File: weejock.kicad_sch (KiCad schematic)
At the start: 44 parts, among them J2 JST-PH2, K1 PG1350, K10 PG1350, K11 PG1350, K12 PG1350, K13 PG1350, K14 PG1350, K15 PG1350, K16 PG1350, K17 PG1350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

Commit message: Beginning to assign footprints.
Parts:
- D1, D10, D11, D12, D13, D14, D15, D16, D17, D18, D19, D2, D20, D3, D4, D5, D6, D7, D8, D9: footprint (none) -> Diode_SMD:D_SOD-123
- J2: footprint (none) -> Connector_JST:JST_PH_S2B-PH-SM4-TB_1x02-1MP_P2.00mm_Horizontal
- K1, K10, K11, K12, K13, K14, K15, K16, K17, K18, K19, K2, K20, K3, K4, K5, K6, K7, K8, K9: footprint (none) -> Switch_Keyboard_Kailh:SW_Kailh_Choc_V1
- SW1: footprint (none) -> Button_Switch_SMD:SW_Push_SPST_NO_Alps_SKRK
- SW2: footprint (none) -> Button_Switch_SMD:SW_SPDT_PCM12
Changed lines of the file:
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@@
 			)
 		)
-		(property "Footprint" ""
+		(property "Footprint" "Diode_SMD:D_SOD-123"
 			(at 38.1 58.42 0)
 			(effects
@@
 			)
 		)
-		(property "Footprint" ""
+		(property "Footprint" "Switch_Keyboard_Kailh:SW_Kailh_Choc_V1"
 			(at 88.9 68.58 0)
 			(effects
@@
 			)
 		)
-		(property "Footprint" ""
+		(property "Footprint" "Switch_Keyboard_Kailh:SW_Kailh_Choc_V1"
 			(at 50.8 87.63 0)
 			(effects
@@
 			)
 		)
-		(property "Footprint" ""
+		(property "Footprint" "Diode_SMD:D_SOD-123"
 			(at 76.2 77.47 0)
 			(effects
@@
 			)
 		)
-		(property "Footprint" ""
+		(property "Footprint" "Switch_Keyboard_Kailh:SW_Kailh_Choc_V1"
 			(at 69.85 68.58 0)
 			(effects
@@
 			)
 		)
-		(property "Footprint" ""
+		(property "Footprint" "Diode_SMD:D_SOD-123"
 			(at 38.1 39.37 0)
 			(effects
@@
 			)
 		)
-		(property "Footprint" ""
+		(property "Footprint" "Button_Switch_SMD:SW_Push_SPST_NO_Alps_SKRK"
 			(at 134.62 99.06 0)
 			(effects
@@
 			)
 		)
-		(property "Footprint" ""
+		(property "Footprint" "Diode_SMD:D_SOD-123"
 			(at 38.1 77.47 0)
 			(effects
@@
 			)
 		)
-		(property "Footprint" ""
+		(property "Footprint" "Diode_SMD:D_SOD-123"
 			(at 76.2 58.42 0)
 			(effects
@@
 			)
 		)
-		(property "Footprint" ""
+		(property "Footprint" "Switch_Keyboard_Kailh:SW_Kailh_Choc_V1"
 			(at 88.9 49.53 0)
 			(effects
@@
 			)
 		)
-		(property "Footprint" ""
+		(property "Footprint" "Connector_JST:JST_PH_S2B-PH-SM4-TB_1x02-1MP_P2.00mm_Horizontal"
 			(at 190.5 107.95 0)
 			(effects
@@
 			)
 		)
-		(property "Footprint" ""
+		(property "Footprint" "Diode_SMD:D_SOD-123"
 			(at 38.1 96.52 0)
 			(effects
@@
 			)
 		)
-		(property "Footprint" ""
+		(property "Footprint" "Diode_SMD:D_SOD-123"
 			(at 95.25 39.37 0)
 			(effects
@@
 			)
 		)
-		(property "Footprint" ""
+		(property "Footprint" "Diode_SMD:D_SOD-123"
 			(at 76.2 115.57 0)
 			(effects
@@
 			)
 		)
-		(property "Footprint" ""
+		(property "Footprint" "Switch_Keyboard_Kailh:SW_Kailh_Choc_V1"
 			(at 50.8 106.68 0)
 			(effects
@@
 			)
 		)
-		(property "Footprint" ""
+		(property "Footprint" "Diode_SMD:D_SOD-123"
 			(at 95.25 77.47 0)
 			(effects
@@
 			)
 		)
-		(property "Footprint" ""
+		(property "Footprint" "Switch_Keyboard_Kailh:SW_Kailh_Choc_V1"
 			(at 69.85 49.53 0)
 			(effects
@@
 			)
 		)
-		(property "Footprint" ""
+		(property "Footprint" "Switch_Keyboard_Kailh:SW_Kailh_Choc_V1"
 			(at 50.8 68.58 0)
 			(effects
@@
 			)
 		)
-		(property "Footprint" ""
+		(property "Footprint" "Diode_SMD:D_SOD-123"
 			(at 76.2 96.52 0)
 			(effects
@@
 			)
 		)
-		(property "Footprint" ""
+		(property "Footprint" "Switch_Keyboard_Kailh:SW_Kailh_Choc_V1"
 			(at 69.85 30.48 0)
 			(effects
@@
 			)
 		)
-		(property "Footprint" ""
+		(property "Footprint" "Switch_Keyboard_Kailh:SW_Kailh_Choc_V1"
 			(at 31.75 49.53 0)
 			(effects
@@
 			)
 		)
-		(property "Footprint" ""
+		(property "Footprint" "Diode_SMD:D_SOD-123"
 			(at 57.15 96.52 0)
 			(effects
@@
 			)
 		)
-		(property "Footprint" ""
+		(property "Footprint" "Switch_Keyboard_Kailh:SW_Kailh_Choc_V1"
 			(at 50.8 30.48 0)
 			(effects
@@
 			)
 		)
-		(property "Footprint" ""
+		(property "Footprint" "Diode_SMD:D_SOD-123"
 			(at 95.25 96.52 0)
 			(effects
@@
 			)
 		)
-		(property "Footprint" ""
+		(property "Footprint" "Diode_SMD:D_SOD-123"
 			(at 57.15 58.42 0)
 			(effects
@@
 			)
 		)
-		(property "Footprint" ""
+		(property "Footprint" "Switch_Keyboard_Kailh:SW_Kailh_Choc_V1"
 			(at 31.75 68.58 0)
 			(effects
@@
 	)
 	(symbol
+		(lib_name "PG1350_1")
 		(lib_id "weejock_keyboard_parts:PG1350")
 		(at 31.75 35.56 0)
@@
 			)
 		)
-		(property "Footprint" ""
+		(property "Footprint" "Switch_Keyboard_Kailh:SW_Kailh_Choc_V1"
 			(at 31.75 30.48 0)
 			(effects
@@
 			)
 		)
-		(property "Footprint" ""
+		(property "Footprint" "Diode_SMD:D_SOD-123"
 			(at 95.25 58.42 0)
 			(effects
@@
 			)
 		)
-		(property "Footprint" ""
+		(property "Footprint" "Switch_Keyboard_Kailh:SW_Kailh_Choc_V1"
 			(at 88.9 87.63 0)
 			(effects
@@
 			)
 		)
-		(property "Footprint" ""
+		(property "Footprint" "Diode_SMD:D_SOD-123"
 			(at 57.15 77.47 0)
 			(effects
@@
 			)
 		)
-		(property "Footprint" ""
+		(property "Footprint" "Diode_SMD:D_SOD-123"
 			(at 57.15 115.57 0)
 			(effects
@@
 			)
 		)
-		(property "Footprint" ""
+		(property "Footprint" "Switch_Keyboard_Kailh:SW_Kailh_Choc_V1"
 			(at 69.85 106.68 0)
 			(effects
@@
 			)
 		)
-		(property "Footprint" ""
+		(property "Footprint" "Diode_SMD:D_SOD-123"
 			(at 38.1 115.57 0)
 			(effects
@@
 			)
 		)
-		(property "Footprint" ""
+		(property "Footprint" "Button_Switch_SMD:SW_SPDT_PCM12"
 			(at 177.8 105.41 0)
 			(effects
@@
 			)
 		)
-		(property "Footprint" ""
+		(property "Footprint" "Diode_SMD:D_SOD-123"
 			(at 76.2 39.37 0)
 			(effects
@@
 			)
 		)
-		(property "Footprint" ""
+		(property "Footprint" "Switch_Keyboard_Kailh:SW_Kailh_Choc_V1"
 			(at 69.85 87.63 0)
 			(effects
@@
 			)
 		)
-		(property "Footprint" ""
+		(property "Footprint" "Switch_Keyboard_Kailh:SW_Kailh_Choc_V1"
 			(at 88.9 106.68 0)
 			(effects
@@
 			)
 		)
-		(property "Footprint" ""
+		(property "Footprint" "Switch_Keyboard_Kailh:SW_Kailh_Choc_V1"
 			(at 31.75 106.68 0)
 			(effects
@@
 			)
 		)
-		(property "Footprint" ""
+		(property "Footprint" "Switch_Keyboard_Kailh:SW_Kailh_Choc_V1"
 			(at 88.9 30.48 0)
 			(effects
@@
 			)
 		)
-		(property "Footprint" ""
+		(property "Footprint" "Switch_Keyboard_Kailh:SW_Kailh_Choc_V1"
 			(at 31.75 87.63 0)
 			(effects
@@
 			)
 		)
-		(property "Footprint" ""
+		(property "Footprint" "Diode_SMD:D_SOD-123"
 			(at 95.25 115.57 0)
 			(effects
@@
 			)
 		)
-		(property "Footprint" ""
+		(property "Footprint" "Switch_Keyboard_Kailh:SW_Kailh_Choc_V1"
 			(at 50.8 49.53 0)
 			(effects
@@
 			)
 		)
-		(property "Footprint" ""
+		(property "Footprint" "Diode_SMD:D_SOD-123"
 			(at 57.15 39.37 0)
 			(effects

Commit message: Fixing up footprints for better routing and access around XIAO.
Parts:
- U1: footprint Seeed Studio XIAO Series Library:XIAO-nRF52840-Sense-14P-2.54-21X17.8MM -> weejock_library:Seeed XIAO Simplified
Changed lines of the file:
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@@
 			)
 		)
-		(property "Footprint" "Seeed Studio XIAO Series Library:XIAO-nRF52840-Sense-14P-2.54-21X17.8MM"
+		(property "Footprint" "weejock_library:Seeed XIAO Simplified"
 			(at 147.32 45.72 0)
 			(effects

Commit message: Version 0.0.2 - use footprint that is both SMT and through hole friendly, and fix JST footprint.
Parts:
- J2: footprint Connector_JST:JST_PH_S2B-PH-SM4-TB_1x02-1MP_P2.00mm_Horizontal -> Connector_JST:JST_PH_S2B-PH-K_1x02_P2.00mm_Horizontal
- K1, K10, K11, K12, K13, K14, K15, K16, K17, K18, K19, K2, K20, K3, K4, K5, K6, K7, K8, K9: footprint Switch_Keyboard_Kailh:SW_Kailh_Choc_V1 -> weejock_library:SW_Kailh_Choc_V1
- U1: footprint weejock_library:Seeed XIAO Simplified -> weejock_library:Castellated XIAO with BAT+ and RST
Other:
- note removed: "2024-10-06"
- note removed: "Wee Jock Grid Pad"
- note removed: "v0.0.1"
- title: (none) -> Wee Jock Grid Pad

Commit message: Minor changes, I think due to moving some text.
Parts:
- SW1: footprint Button_Switch_SMD:SW_Push_SPST_NO_Alps_SKRK -> Button_Switch_SMD:SW_SPST_B3U-1000P
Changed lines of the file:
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@@
 			)
 		)
-		(property "Footprint" "Button_Switch_SMD:SW_Push_SPST_NO_Alps_SKRK"
+		(property "Footprint" "Button_Switch_SMD:SW_SPST_B3U-1000P"
 			(at 134.62 99.06 0)
 			(effects

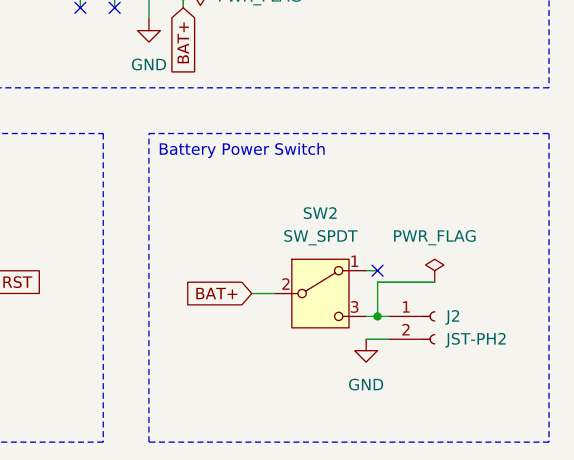
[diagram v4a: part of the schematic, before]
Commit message: Rev 3: Fix up pad placement and silkscreen labels, as well as repositioning components a little. (#5)
* Correcting XIAO BLE footprint to reverse accidental mirroring of pads.

* Neatening power switch and adding ON/OFF labels.

* Labeling reset button.

* Moving JST jack for better keycap clearance, and adding +/- labels.

* Messing with labels.

* Update sheet metadata to reflect version number 0.0.3
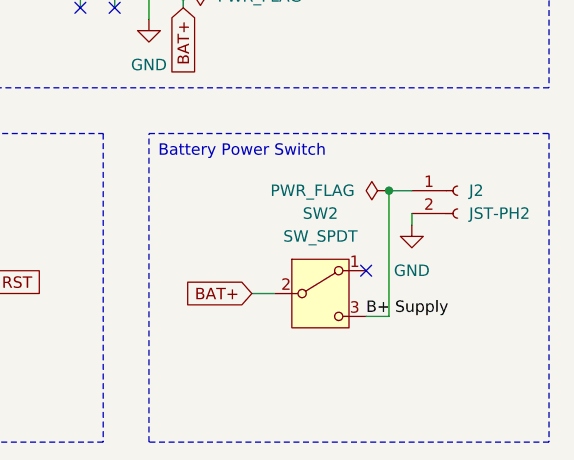
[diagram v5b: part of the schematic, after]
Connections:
- net B+ Supply: now reaches J2.1 (Pin_1), SW2.3 (C)
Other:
- moved on the sheet: J2
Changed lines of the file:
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@@
 	(title_block
 		(title "Wee Jock Grid Pad")
-		(date "2024-10-10")
-		(rev "v0.0.2")
+		(date "2024-10-17")
+		(rev "v0.0.3")
 	)
 	(junction
@@
 	)
 	(junction
-		(at 82.55 54.61)
+		(at 185.42 93.98)
 		(diameter 0)
 		(color 0 0 0 0)
 	)
 	(junction
-		(at 57.15 81.28)
+		(at 82.55 54.61)
 		(diameter 0)
 		(color 0 0 0 0)
 	)
 	(junction
-		(at 184.15 107.95)
+		(at 57.15 81.28)
 		(diameter 0)
 		(color 0 0 0 0)
@@
 	)
 	(no_connect
-		(at 184.15 102.87)
-	)
-	(no_connect
 		(at 177.8 46.99)
 	)
@@
 	)
 	(no_connect
+		(at 182.88 102.87)
+	)
+	(no_connect
 		(at 154.94 26.67)
 	)
@@
 	(wire
 		(pts
-			(xy 190.5 104.14) (xy 184.15 104.14)
+			(xy 25.4 54.61) (xy 26.67 54.61)
 		)
 		(stroke
@@
 	(wire
 		(pts
-			(xy 25.4 54.61) (xy 26.67 54.61)
+			(xy 44.45 92.71) (xy 44.45 111.76)
 		)
 		(stroke
@@
 	(wire
 		(pts
-			(xy 44.45 92.71) (xy 44.45 111.76)
+			(xy 95.25 100.33) (xy 102.87 100.33)
 		)
 		(stroke
@@
 	(wire
 		(pts
-			(xy 95.25 100.33) (xy 102.87 100.33)
+			(xy 44.45 92.71) (xy 45.72 92.71)
 		)
 		(stroke
@@
 	(wire
 		(pts
-			(xy 44.45 92.71) (xy 45.72 92.71)
+			(xy 130.81 54.61) (xy 134.62 54.61)
 		)
 		(stroke
@@
 	(wire
 		(pts
-			(xy 130.81 54.61) (xy 134.62 54.61)
+			(xy 44.45 35.56) (xy 45.72 35.56)
 		)
 		(stroke
@@
 	(wire
 		(pts
-			(xy 44.45 35.56) (xy 45.72 35.56)
+			(xy 185.42 93.98) (xy 185.42 107.95)
 		)
 		(stroke
@@
 	(wire
 		(pts
-			(xy 182.88 107.95) (xy 184.15 107.95)
+			(xy 25.4 54.61) (xy 25.4 73.66)
 		)
 		(stroke
@@
 	(wire
 		(pts
-			(xy 25.4 54.61) (xy 25.4 73.66)
+			(xy 95.25 62.23) (xy 102.87 62.23)
 		)
 		(stroke
@@
 	(wire
 		(pts
-			(xy 95.25 62.23) (xy 102.87 62.23)
+			(xy 74.93 54.61) (xy 76.2 54.61)
 		)
 		(stroke
@@
 	(wire
 		(pts
-			(xy 74.93 54.61) (xy 76.2 54.61)
+			(xy 182.88 107.95) (xy 185.42 107.95)
 		)
 		(stroke
@@
 	(wire
 		(pts
-			(xy 95.25 119.38) (xy 102.87 119.38)
-		)
-		(stroke
-			(width 0)
-			(type default)
-		)
-	)
-	(wire
-		(pts
-			(xy 63.5 35.56) (xy 64.77 35.56)
+			(xy 187.96 97.79) (xy 187.96 96.52)
 		)
 		(stroke
@@
 	(wire
 		(pts
-			(xy 63.5 92.71) (xy 64.77 92.71)
+			(xy 95.25 119.38) (xy 102.87 119.38)
 		)
 		(stroke
@@
 	(wire
 		(pts
-			(xy 139.7 104.14) (xy 140.97 104.14)
+			(xy 63.5 35.56) (xy 64.77 35.56)
 		)
 		(stroke
@@
 	(wire
 		(pts
-			(xy 182.88 110.49) (xy 185.42 110.49)
+			(xy 63.5 92.71) (xy 64.77 92.71)
 		)
 		(stroke
@@
 	(wire
 		(pts
-			(xy 184.15 104.14) (xy 184.15 107.95)
+			(xy 139.7 104.14) (xy 140.97 104.14)
 		)
 		(stroke
@@
 	(wire
 		(pts
-			(xy 184.15 102.87) (xy 182.88 102.87)
-		)
-		(stroke
-			(width 0)
-			(type default)
-		)
-	)
-	(wire
-		(pts
 			(xy 63.5 73.66) (xy 63.5 92.71)
 		)
@@
 	(wire
 		(pts
+			(xy 185.42 93.98) (xy 187.96 93.98)
+		)
+		(stroke
+			(width 0)
+			(type default)
+		)
+	)
+	(wire
+		(pts
 			(xy 36.83 35.56) (xy 38.1 35.56)
 		)
@@
 	(wire
 		(pts
-			(xy 184.15 107.95) (xy 185.42 107.95)
-		)
-		(stroke
-			(width 0)
-			(type default)
-		)
-	)
-	(wire
-		(pts
 			(xy 130.81 50.8) (xy 134.62 50.8)
 		)
@@
 		)
 	)
+	(label "B+ Supply"
+		(at 182.88 107.95 0)
+		(effects
+			(font
+				(size 1.27 1.27)
+			)
+			(justify left bottom)
+		)
+	)
 	(global_label "RST"
 		(shape input)
@@
 	(symbol
 		(lib_id "weejock_keyboard_parts:JST-PH2")
-		(at 190.5 107.95 0)
+		(at 193.04 93.98 0)
 		(unit 1)
 		(exclude_from_sim no)
@@
 		(fields_autoplaced yes)
 		(property "Reference" "J2"
-			(at 191.77 107.9499 0)
+			(at 194.31 93.9799 0)
 			(effects
 				(font
@@
 		)
 		(property "Value" "JST-PH2"
-			(at 191.77 110.4899 0)
+			(at 194.31 96.5199 0)
 			(effects
 				(font
@@
 		)
 		(property "Footprint" "Connector_JST:JST_PH_S2B-PH-K_1x02_P2.00mm_Horizontal"
-			(at 190.5 107.95 0)
+			(at 193.04 93.98 0)
 			(effects
 				(font
@@
 		)
 		(property "Datasheet" "~"
-			(at 190.5 107.95 0)
+			(at 193.04 93.98 0)
 			(effects
 				(font
@@
 		)
 		(property "Description" "Generic connector, single row, 01x02, script generated"
-			(at 190.5 107.95 0)
+			(at 193.04 93.98 0)
 			(effects
 				(font
@@
 	(symbol
 		(lib_id "power:PWR_FLAG")
-		(at 190.5 104.14 0)
+		(at 185.42 93.98 90)
 		(unit 1)
 		(exclude_from_sim no)
@@
 		(fields_autoplaced yes)
 		(property "Reference" "#FLG01"
-			(at 190.5 102.235 0)
+			(at 183.515 93.98 0)
 			(effects
 				(font
@@
 		)
 		(property "Value" "PWR_FLAG"
-			(at 190.5 99.06 0)
+			(at 181.61 93.9799 90)
 			(effects
 				(font
 					(size 1.27 1.27)
 				)
+				(justify left)
 			)
 		)
 		(property "Footprint" ""
-			(at 190.5 104.14 0)
+			(at 185.42 93.98 0)
 			(effects
 				(font
@@
 		)
 		(property "Datasheet" "~"
-			(at 190.5 104.14 0)
+			(at 185.42 93.98 0)
 			(effects
 				(font
@@
 		)
 		(property "Description" "Special symbol for telling ERC where power comes from"
-			(at 190.5 104.14 0)
+			(at 185.42 93.98 0)
 			(effects
 				(font
@@
 	(symbol
 		(lib_id "power:GND")
-		(at 182.88 110.49 0)
+		(at 187.96 97.79 0)
 		(unit 1)
 		(exclude_from_sim no)
@@
 		(fields_autoplaced yes)
 		(property "Reference" "#PWR04"
-			(at 182.88 116.84 0)
+			(at 187.96 104.14 0)
 			(effects
 				(font
@@
 		)
 		(property "Value" "GND"
-			(at 182.88 115.57 0)
+			(at 187.96 102.87 0)
 			(effects
 				(font
@@
 		)
 		(property "Footprint" ""
-			(at 182.88 110.49 0)
+			(at 187.96 97.79 0)
 			(effects
 				(font
@@
 		)
 		(property "Datasheet" ""
-			(at 182.88 110.49 0)
+			(at 187.96 97.79 0)
 			(effects
 				(font
@@
 		)
 		(property "Description" "Power symbol creates a global label with name \"GND\" , ground"
-			(at 182.88 110.49 0)
+			(at 187.96 97.79 0)
 			(effects
 				(font
